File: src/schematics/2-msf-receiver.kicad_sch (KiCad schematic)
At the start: 16 parts, among them U2 TPS7A2036PDBVR, U5 TPS7A2040PDQNR

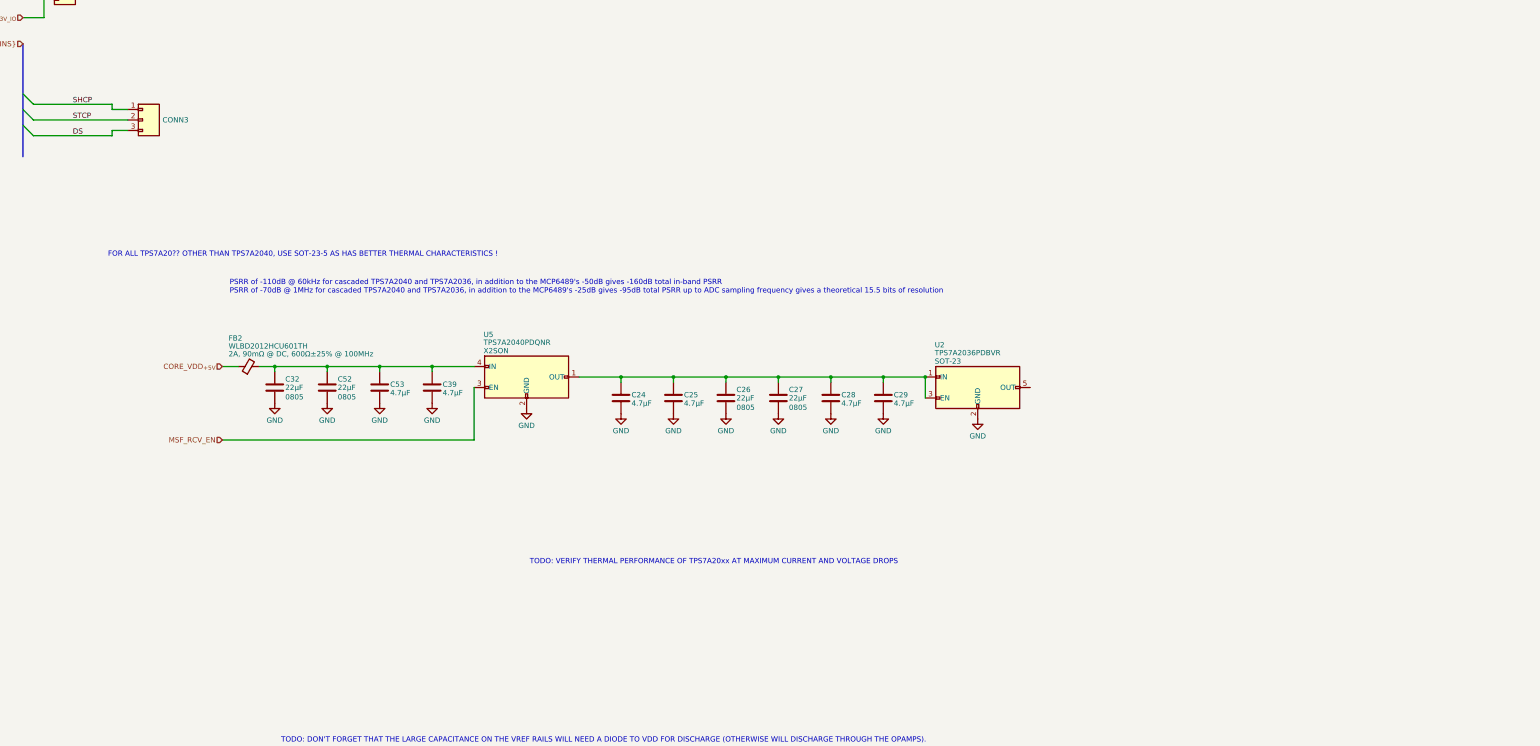
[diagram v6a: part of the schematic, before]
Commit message: Lots of faffing around trying to get ngspice to (reliably) converge for the MSF front-end, particularly around the Monte-Carlo simulations which seem to diverge for some values - it even appears as though some state is being held onto / corrupted between plots.  A good range of values has been tested and they agree nicely with each other, however.  Enough confidence exists to build it.  Also selected a new op-amp and removed the AZ431 voltage reference in favour of an op-amp solution, based on feedback from the simulations.  Noise and dynamic range estimations are satisfactory for this application, ADC and filter order.
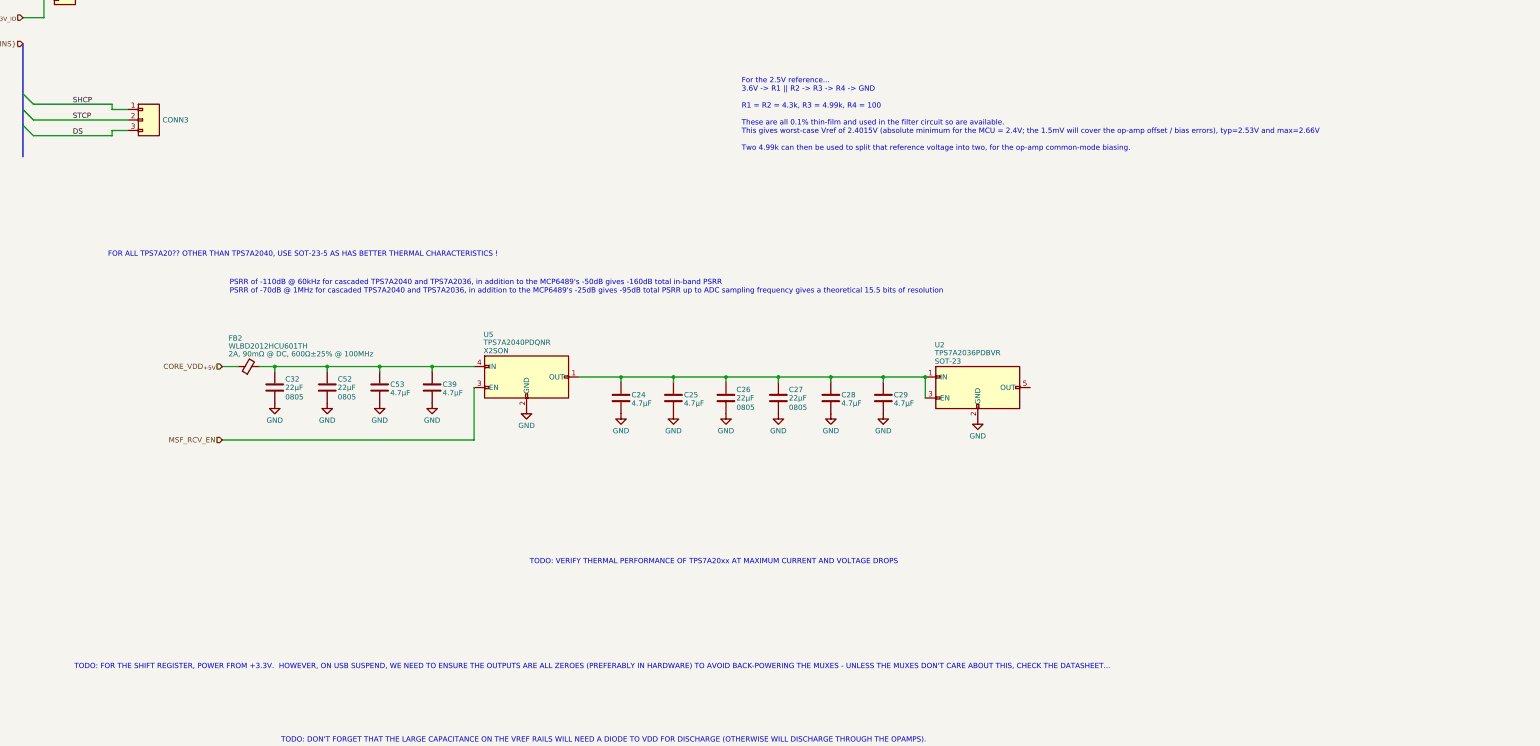
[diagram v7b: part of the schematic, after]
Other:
- note added: "For the 2.5V reference... 3.6V -> R1 || R2 -> R3 -> R4 -> GND R1 = R2 = 4.3k, R3 = 4.99k, R4 = 100 These are all 0.1% thin-film and used in the filter circuit so are available. This gives worst-case Vref of 2.4015V (absolute minimum for the MCU = 2.4V; the 1.5mV will cover the op-amp offset / bias errors), typ=2.53V and max=2.66V Two 4.99k can then be used to split that reference voltage into two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"
- note added: "TODO: FOR THE SHIFT REGISTER, POWER FROM +3.3V. HOWEVER, ON USB SUSPEND, WE NEED TO ENSURE THE OUTPUTS ARE ALL ZEROES (PREFERABLY IN HARDWARE) TO AVOID BACK-POWERING THE MUXES - UNLESS THE MUXES DON'T CARE ABOUT THIS, CHECK THE DATASHEET..."
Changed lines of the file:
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@@
+    (effects (font (size 1.27 1.27)) (justify left bottom))
+  )
+  (text "TODO: FOR THE SHIFT REGISTER, POWER FROM +3.3V.  HOWEVER, ON USB SUSPEND, WE NEED TO ENSURE THE OUTPUTS ARE ALL ZEROES (PREFERABLY IN HARDWARE) TO AVOID BACK-POWERING THE MUXES - UNLESS THE MUXES DON'T CARE ABOUT THIS, CHECK THE DATASHEET..."
+    (at 50.546 225.806 0)
     (effects (font (size 1.27 1.27)) (justify left bottom))
   )
@@
     (effects (font (size 1.27 1.27)) (justify left bottom))
   )
+  (text "For the 2.5V reference...\n3.6V -> R1 || R2 -> R3 -> R4 -> GND\n\nR1 = R2 = 4.3k, R3 = 4.99k, R4 = 100\n\nThese are all 0.1% thin-film and used in the filter circuit so are available.\nThis gives worst-case Vref of 2.4015V (absolute minimum for the MCU = 2.4V; the 1.5mV will cover the op-amp offset / bias errors), typ=2.53V and max=2.66V\n\nTwo 4.99k can then be used to split that reference voltage into two, for the op-amp common-mode biasing."
+    (at 212.09 100.33 0)
+    (effects (font (size 1.27 1.27)) (justify left bottom))
+  )

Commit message: Started to draw the MSF receiver based on the simulation learnings.
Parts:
- added C30, C33, C40, C41, C49: 4.7μF, restall-generic-capacitors:unpolarised-nominal-0402-1005, symbol restall-generic-capacitors:capacitor-unpolarised
- added C31, C34, C38: DNP, restall-generic-capacitors:unpolarised-nominal-0805-2012, symbol restall-generic-capacitors:capacitor-unpolarised
- added C35, C36, C37: 22μF, restall-generic-capacitors:unpolarised-nominal-0805-2012, symbol restall-generic-capacitors:capacitor-unpolarised
- added C43, C48: DNP, restall-generic-capacitors:unpolarised-nominal-0402-1005, symbol restall-generic-capacitors:capacitor-unpolarised
- added C44, C47: 470pF, restall-generic-capacitors:unpolarised-nominal-0402-1005, symbol restall-generic-capacitors:capacitor-unpolarised
- added C45, C46, C50, C51: 4.7nF, restall-generic-capacitors:unpolarised-nominal-0603-1608, symbol restall-generic-capacitors:capacitor-unpolarised
- added D10, D11, D8, D9: SD103AWS, restall-generic-sot:SOD-323, symbol restall-generic-diodes:schottky
- added R22, R24: 4.3kΩ, restall-generic-resistors:nominal-0402-1005, symbol restall-generic-resistors:resistor
- added R23, R28, R30, R38, R50: 4.99kΩ, restall-generic-resistors:nominal-0402-1005, symbol restall-generic-resistors:resistor
- added R25, R27: 27Ω, restall-generic-resistors:nominal-0402-1005, symbol restall-generic-resistors:resistor
- added R26, R29: DNP, restall-generic-resistors:nominal-0402-1005, symbol restall-generic-resistors:resistor
- added R31, R32, R42, R44: 0Ω, restall-generic-resistors:nominal-0402-1005, symbol restall-generic-resistors:resistor
- added R33, R35, R47: 390Ω, restall-generic-resistors:nominal-0402-1005, symbol restall-generic-resistors:resistor
- added R34: 47Ω, restall-generic-resistors:nominal-0402-1005, symbol restall-generic-resistors:resistor
- added R36, R48: 1.24kΩ, restall-generic-resistors:nominal-0402-1005, symbol restall-generic-resistors:resistor
- added R37, R49, R52, R53, R54, R55, R56, R57, R59: 2.49kΩ, restall-generic-resistors:nominal-0402-1005, symbol restall-generic-resistors:resistor
- added R39, R45: 4.12kΩ, restall-generic-resistors:nominal-0402-1005, symbol restall-generic-resistors:resistor
- added R40, R46: 64.9Ω, restall-generic-resistors:nominal-0402-1005, symbol restall-generic-resistors:resistor
- added R41, R43: 49.9kΩ, restall-generic-resistors:nominal-0402-1005, symbol restall-generic-resistors:resistor
- added R51: 100Ω, restall-generic-resistors:nominal-0402-1005, symbol restall-generic-resistors:resistor
- added R58, R60: 68Ω, restall-generic-resistors:nominal-0402-1005, symbol restall-generic-resistors:resistor
- added U203, U204: MCP6499, restall-manufacturer-microchip:SOIC14-3.9x8.65mm-1.27mm, symbol restall-manufacturer-microchip:MCP6499?-?-S?
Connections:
- net GND: now also C30.2, C33.2, C35.2, C36.2, C37.2, C38.2, C40.2, C41.2, C49.2, R23.2, R28.2, R40.2, R46.2, U203.11 (V_{SS}), U204.11 (V_{SS})
- net MSF_ANT_{+}: now also R33.1; no longer CONN1.1 (P1)
- net MSF_ANT_{-}: now also C35.1, C36.1, C37.1, C38.1, C40.1, C41.1, C49.1, D10.2 (A), R27.2, R29.2, R34.2, R51.2, R52.2, U203.12 (+), U204.10 (+); no longer CONN1.2 (P2)
- net MSF_OUT_{+}: now also R58.2; no longer CONN2.1 (P1)
- net MSF_OUT_{-}: now also R60.2; no longer CONN2.2 (P2)
- net MSF_VDD_{+3.6V}: now reaches U2.5 (OUT)
- net MSF_VDD_{+3.6V}: now also D10.1 (K), D11.1 (K), D8.1 (K), D9.1 (K), R22.1, R24.1, R30.1
- new net: C51.1, R59.1
- new net: C30.1, D8.2 (A), R22.2, R23.1, R24.2, U203.5 (+)
- new net: R41.2, R42.1
- new net: C46.1, C47.1, R45.2, R46.1
- new net: C34.2, R27.1, R32.2, U203.8
- new net: C34.1, R29.1, R32.1, U203.9 (-)
- new net: C33.1, D9.2 (A), R28.1, R30.2, U203.10 (+)
- new net: C44.1, C45.1, R39.2, R40.1
- new net: C47.2, R44.2, U204.9 (-)
- new net: R33.2, U203.3 (+)
- new net: C31.1, R26.1, R31.1, U203.6 (-)
- new net: R54.2, R56.2, R58.1, U204.1
- new net: R54.1, R55.1, U204.2 (-)
- new net: R53.1, R59.2, U204.3 (+)
- new net: R56.1, R57.1, U204.13 (-)
- new net: R53.2, R55.2, R57.2, R60.1, U204.14
- new net: R43.2, R44.1
- new net: C31.2, R25.1, R31.2, U203.7
- new net: C50.1, R52.1, U204.5 (+)
- new net: C44.2, R42.2, U203.13 (-)
- new net FB0: C43.1, C48.1, R34.1, R35.1, R47.1, R51.1, U203.2 (-), U204.6 (-)
- new net FB1: R35.2, R36.1, R47.2, R48.1
- new net FB2: R36.2, R37.1, R48.2, R49.1
- new net FB3: R37.2, R38.1, R49.2, R50.1
- new net FB4: C43.2, C48.2, R38.2, R39.1, R45.1, R50.2, U203.1, U204.7
- new net MSF_RCV_TRF1: C45.2, C50.2, R41.1, U203.14
- new net MSF_RCV_TRF2: C46.2, R43.1, U204.8
- new net MSF_RCV_VREF_{+2.5V}: D11.2 (A), R25.2, R26.2
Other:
- note added: "Estimated from the datasheets, the in-band PSRR@60kHz is around -130dB (the TPS7A2040 around -30dB, TPS7A2036 around -50dB, the MCP6499 around -50dB). The maximum ripple on the +5V rail when used at a maximum gain of 88.6dB is 18mV_{rms}, which keeps the noise at the end of the signal chain about -6dB below the signal chain's (ie. op-amp's) noise; 19.1μV_{rms} / 3.3mV_{rms} for minimum / maximum 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"
- note added: "MFB Bandpass, f_{0}≃60kHz, Q≃8, K≃-1.1 Split R2xx / R2yy provides opportunity for a Deliyannis topology if desired."
- note added: "Programmable Amplifier, +1.5dB to +39.3dB"
- note added: "Programmable Amplifier, +3.0dB to +45.8dB"
- note added: "Route as length-matched differential lines, Z_{0}=68Ω ADC V_{fs}≃±2.5V_{p-p}-7% headroom ADC V_{cm}≃1.25V"
- note added: "Single-Ended-to-Differential Bridge with equalised output delays. See Op-Amps for Everyone, p269."
- note added: "TODO: 1.25V vref (don't forget diode discharge !)"
- note added: "TODO: 1.8V OUT"
- note added: "TODO: ADD SWITCHES"
- note added: "TODO: BYPASS CAPACITORS !"
- note added: "TODO: BYPASS CAPS"
- note added: "Tuned RF Secion 1"
- note added: "Tuned RF Secion 2"
- note added: "U203B/C - Topology for large capacitive load compensation. Calculations can be found in Op-Amps for Everyone, p287."
- note added: "Unless otherwise specified: All resistors and capacitors are 0402 All resistors are ±1% 100ppm 0.625W thick-film All capacitors are ±20% X5R 10V MLCC"
- note removed: "FOR ALL TPS7A20?? OTHER THAN TPS7A2040, USE SOT-23-5 AS HAS BETTER THERMAL CHARACTERISTICS !"
- note removed: "For the 2.5V reference... 3.6V -> R1 || R2 -> R3 -> R4 -> GND R1 = R2 = 4.3k, R3 = 4.99k, R4 = 100 These are all 0.1% thin-film and used in the filter circuit so are available. This gives worst-case Vref of 2.4015V (absolute minimum for the MCU = 2.4V; the 1.5mV will cover the op-amp offset / bias errors), typ=2.53V and max=2.66V Two 4.99k can then be used to split that reference voltage into two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"
- note removed: "PSRR of -110dB @ 60kHz for cascaded TPS7A2040 and TPS7A2036, in addition to the MCP6489's -50dB gives -160dB total in-band PSRR PSRR of -70dB @ 1MHz for cascaded TPS7A2040 and TPS7A2036, in addition to the MCP6489's -25dB gives -95dB total PSRR up to ADC sampling frequency gives a theoretical 15.5 bits of resolution"
- note removed: "TODO: 2.2nV of noise is 1/2 LSB at 8483V/V gain, vref=2.48V, 16-bit resolution. PSRR of -50dB for the MCP6489 @ 60kHz PSRR of -60dB for the TPS7A2028 @ 60kHz So ripple at 60kHz must be < 10^{110 / 20} * 2.2*10^{-9} < 705uV ! Or ripple < 2.8mV for 14-bit resolution. 2.48 / 2^{16} / 2 = 18uV 18uV / 8483 = 2.2nV 2.2nV * 10^{110 / 20} = 705uV With input rail ripple of +/-50mV at 60kHz, a further redu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"
- note removed: "TODO: VERIFY THERMAL PERFORMANCE OF TPS7A20xx AT MAXIMUM CURRENT AND VOLTAGE DROPS"
- moved on the sheet: C24, C25, C26, C27, C28, C29, C32, C39, C52, C53, FB2, U2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
